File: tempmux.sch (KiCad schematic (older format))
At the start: 23 parts, among them J3 Conn_02x07_Counter_Clockwise, U12 CD74HC4067SM

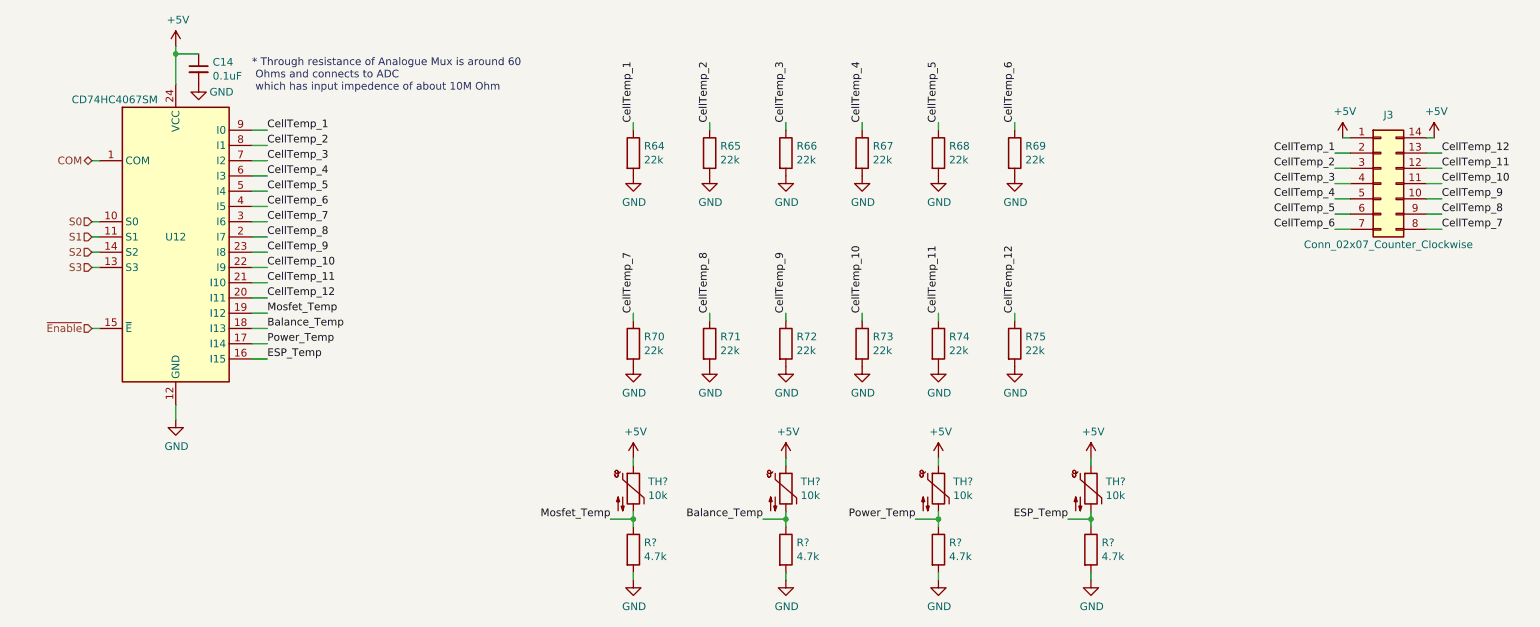
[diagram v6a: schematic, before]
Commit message: Added most footprints
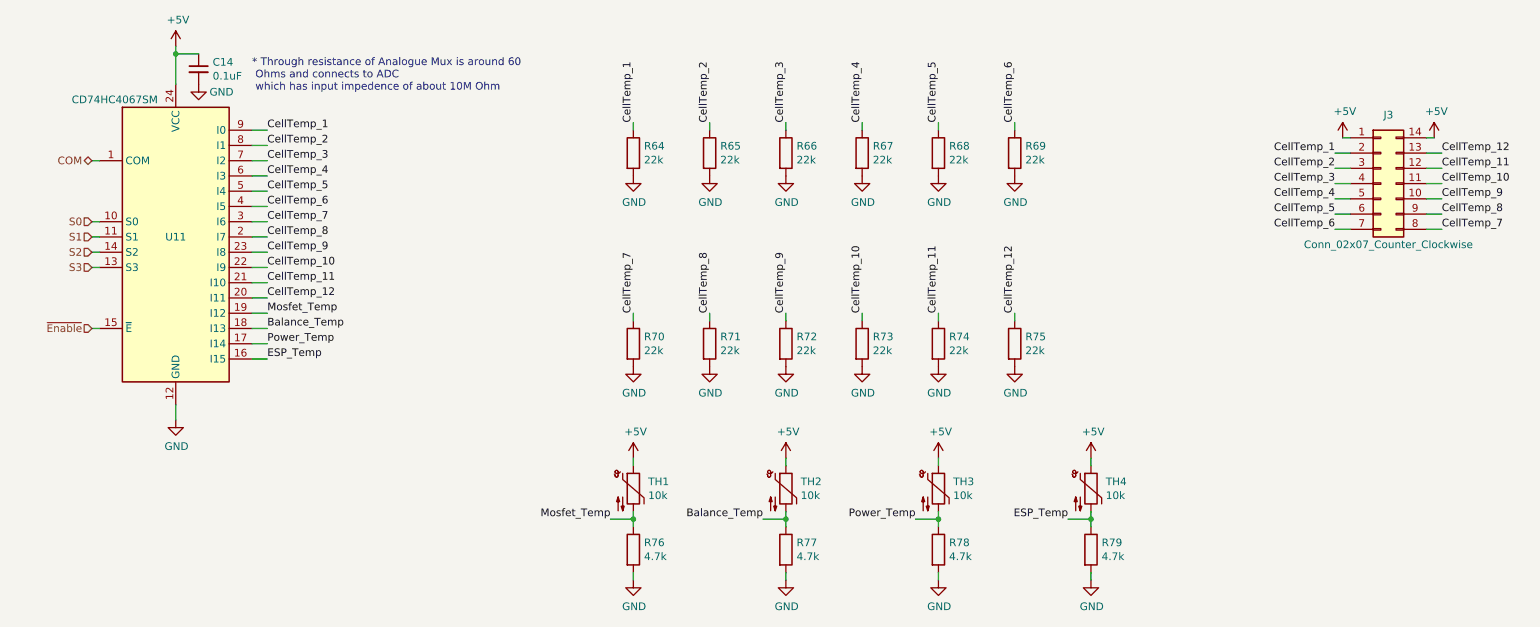
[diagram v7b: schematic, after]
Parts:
- C14: footprint (none) -> Capacitor_SMD:C_1206_3216Metric
- J3: footprint (none) -> Connector_PinHeader_2.54mm:PinHeader_2x07_P2.54mm_Vertical
- R64, R65, R66, R67, R68, R69, R70, R71, R72, R73, R74, R75: footprint (none) -> Resistor_SMD:R_0603_1608Metric_Pad1.05x0.95mm_HandSolder
- R76, R77, R78, R79: renamed from R?; footprint (none) -> Resistor_SMD:R_0603_1608Metric_Pad1.05x0.95mm_HandSolder
- TH1, TH2, TH3, TH4: renamed from TH?; footprint (none) -> Resistor_SMD:R_0201_0603Metric
- renumbered U12 to U11
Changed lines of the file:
@@
 P 2000 2200
 AR Path="/5F70A721/5F6868D3" Ref="U?"  Part="1"
-AR Path="/5F70B1A3/5F6868D3" Ref="U12"  Part="1"
-F 0 "U12" H 2000 2200 50  0000 C CNN
+AR Path="/5F70B1A3/5F6868D3" Ref="U11"  Part="1"
+F 0 "U11" H 2000 2200 50  0000 C CNN
 F 1 "CD74HC4067SM" H 1600 3100 50  0000 C CNN
 F 2 "Package_SO:SSOP-24_5.3x8.2mm_P0.65mm" H 3050 1200 50  0001 C CIN
@@
 F 0 "C14" H 2242 1146 50  0000 L CNN
 F 1 "0.1uF" H 2242 1055 50  0000 L CNN
-F 2 "" H 2150 1100 50  0001 C CNN
+F 2 "Capacitor_SMD:C_1206_3216Metric" H 2150 1100 50  0001 C CNN
 F 3 "~" H 2150 1100 50  0001 C CNN
 	1    2150 1100
@@
 F 0 "J3" H 9950 2300 50  0000 C CNN
 F 1 "Conn_02x07_Counter_Clockwise" H 9950 1450 50  0000 C CNN
-F 2 "" H 9900 1850 50  0001 C CNN
+F 2 "Connector_PinHeader_2.54mm:PinHeader_2x07_P2.54mm_Vertical" H 9900 1850 50  0001 C CNN
 F 3 "~" H 9900 1850 50  0001 C CNN
 	1    9900 1850
@@
 F 0 "R64" H 5070 1696 50  0000 L CNN
 F 1 "22k" H 5070 1605 50  0000 L CNN
-F 2 "" V 4930 1650 50  0001 C CNN
+F 2 "Resistor_SMD:R_0603_1608Metric_Pad1.05x0.95mm_HandSolder" V 4930 1650 50  0001 C CNN
 F 3 "~" H 5000 1650 50  0001 C CNN
 	1    5000 1650
@@
 F 0 "R65" H 5570 1696 50  0000 L CNN
 F 1 "22k" H 5570 1605 50  0000 L CNN
-F 2 "" V 5430 1650 50  0001 C CNN
+F 2 "Resistor_SMD:R_0603_1608Metric_Pad1.05x0.95mm_HandSolder" V 5430 1650 50  0001 C CNN
 F 3 "~" H 5500 1650 50  0001 C CNN
 	1    5500 1650
@@
 F 0 "R66" H 6070 1696 50  0000 L CNN
 F 1 "22k" H 6070 1605 50  0000 L CNN
-F 2 "" V 5930 1650 50  0001 C CNN
+F 2 "Resistor_SMD:R_0603_1608Metric_Pad1.05x0.95mm_HandSolder" V 5930 1650 50  0001 C CNN
 F 3 "~" H 6000 1650 50  0001 C CNN
 	1    6000 1650
@@
 F 0 "R67" H 6570 1696 50  0000 L CNN
 F 1 "22k" H 6570 1605 50  0000 L CNN
-F 2 "" V 6430 1650 50  0001 C CNN
+F 2 "Resistor_SMD:R_0603_1608Metric_Pad1.05x0.95mm_HandSolder" V 6430 1650 50  0001 C CNN
 F 3 "~" H 6500 1650 50  0001 C CNN
 	1    6500 1650
@@
 F 0 "R68" H 7070 1696 50  0000 L CNN
 F 1 "22k" H 7070 1605 50  0000 L CNN
-F 2 "" V 6930 1650 50  0001 C CNN
+F 2 "Resistor_SMD:R_0603_1608Metric_Pad1.05x0.95mm_HandSolder" V 6930 1650 50  0001 C CNN
 F 3 "~" H 7000 1650 50  0001 C CNN
 	1    7000 1650
@@
 F 0 "R69" H 7570 1696 50  0000 L CNN
 F 1 "22k" H 7570 1605 50  0000 L CNN
-F 2 "" V 7430 1650 50  0001 C CNN
+F 2 "Resistor_SMD:R_0603_1608Metric_Pad1.05x0.95mm_HandSolder" V 7430 1650 50  0001 C CNN
 F 3 "~" H 7500 1650 50  0001 C CNN
 	1    7500 1650
@@
 F 0 "R70" H 5070 2946 50  0000 L CNN
 F 1 "22k" H 5070 2855 50  0000 L CNN
-F 2 "" V 4930 2900 50  0001 C CNN
+F 2 "Resistor_SMD:R_0603_1608Metric_Pad1.05x0.95mm_HandSolder" V 4930 2900 50  0001 C CNN
 F 3 "~" H 5000 2900 50  0001 C CNN
 	1    5000 2900
@@
 F 0 "R71" H 5570 2946 50  0000 L CNN
 F 1 "22k" H 5570 2855 50  0000 L CNN
-F 2 "" V 5430 2900 50  0001 C CNN
+F 2 "Resistor_SMD:R_0603_1608Metric_Pad1.05x0.95mm_HandSolder" V 5430 2900 50  0001 C CNN
 F 3 "~" H 5500 2900 50  0001 C CNN
 	1    5500 2900
@@
 F 0 "R72" H 6070 2946 50  0000 L CNN
 F 1 "22k" H 6070 2855 50  0000 L CNN
-F 2 "" V 5930 2900 50  0001 C CNN
+F 2 "Resistor_SMD:R_0603_1608Metric_Pad1.05x0.95mm_HandSolder" V 5930 2900 50  0001 C CNN
 F 3 "~" H 6000 2900 50  0001 C CNN
 	1    6000 2900
@@
 F 0 "R73" H 6570 2946 50  0000 L CNN
 F 1 "22k" H 6570 2855 50  0000 L CNN
-F 2 "" V 6430 2900 50  0001 C CNN
+F 2 "Resistor_SMD:R_0603_1608Metric_Pad1.05x0.95mm_HandSolder" V 6430 2900 50  0001 C CNN
 F 3 "~" H 6500 2900 50  0001 C CNN
 	1    6500 2900
@@
 F 0 "R74" H 7070 2946 50  0000 L CNN
 F 1 "22k" H 7070 2855 50  0000 L CNN
-F 2 "" V 6930 2900 50  0001 C CNN
+F 2 "Resistor_SMD:R_0603_1608Metric_Pad1.05x0.95mm_HandSolder" V 6930 2900 50  0001 C CNN
 F 3 "~" H 7000 2900 50  0001 C CNN
 	1    7000 2900
@@
 F 0 "R75" H 7570 2946 50  0000 L CNN
 F 1 "22k" H 7570 2855 50  0000 L CNN
-F 2 "" V 7430 2900 50  0001 C CNN
+F 2 "Resistor_SMD:R_0603_1608Metric_Pad1.05x0.95mm_HandSolder" V 7430 2900 50  0001 C CNN
 F 3 "~" H 7500 2900 50  0001 C CNN
 	1    7500 2900
@@
 	2500 2600 2600 2600
 $Comp
-L Device:Thermistor_NTC TH?
+L Device:Thermistor_NTC TH1
 U 1 1 5F26609F
 P 5000 3850
-F 0 "TH?" H 5097 3896 50  0000 L CNN
+F 0 "TH1" H 5097 3896 50  0000 L CNN
 F 1 "10k" H 5097 3805 50  0000 L CNN
-F 2 "" H 5000 3900 50  0001 C CNN
+F 2 "Resistor_SMD:R_0201_0603Metric" H 5000 3900 50  0001 C CNN
 F 3 "~" H 5000 3900 50  0001 C CNN
 	1    5000 3850
@@
 $EndComp
 $Comp
-L Device:R R?
+L Device:R R76
 U 1 1 5F2670CB
 P 5000 4250
-F 0 "R?" H 5070 4296 50  0000 L CNN
+F 0 "R76" H 5070 4296 50  0000 L CNN
 F 1 "4.7k" H 5070 4205 50  0000 L CNN
-F 2 "" V 4930 4250 50  0001 C CNN
+F 2 "Resistor_SMD:R_0603_1608Metric_Pad1.05x0.95mm_HandSolder" V 4930 4250 50  0001 C CNN
 F 3 "~" H 5000 4250 50  0001 C CNN
 	1    5000 4250
@@
 P 5000 4450
 AR Path="/5F70A721/5F26879D" Ref="#PWR?"  Part="1"
-AR Path="/5F70B1A3/5F26879D" Ref="#PWR?"  Part="1"
-F 0 "#PWR?" H 5000 4200 50  0001 C CNN
+AR Path="/5F70B1A3/5F26879D" Ref="#PWR083"  Part="1"
+F 0 "#PWR083" H 5000 4200 50  0001 C CNN
 F 1 "GND" H 5005 4277 50  0000 C CNN
 F 2 "" H 5000 4450 50  0001 C CNN
@@
 P 5000 3650
 AR Path="/5F70A721/5F269BD4" Ref="#PWR?"  Part="1"
-AR Path="/5F70B1A3/5F269BD4" Ref="#PWR?"  Part="1"
-F 0 "#PWR?" H 5000 3500 50  0001 C CNN
+AR Path="/5F70B1A3/5F269BD4" Ref="#PWR079"  Part="1"
+F 0 "#PWR079" H 5000 3500 50  0001 C CNN
 F 1 "+5V" H 5015 3823 50  0000 C CNN
 F 2 "" H 5000 3650 50  0001 C CNN
@@
 	5000 3650 5000 3700
 $Comp
-L Device:Thermistor_NTC TH?
+L Device:Thermistor_NTC TH2
 U 1 1 5F26E197
 P 6000 3850
-F 0 "TH?" H 6097 3896 50  0000 L CNN
+F 0 "TH2" H 6097 3896 50  0000 L CNN
 F 1 "10k" H 6097 3805 50  0000 L CNN
-F 2 "" H 6000 3900 50  0001 C CNN
+F 2 "Resistor_SMD:R_0201_0603Metric" H 6000 3900 50  0001 C CNN
 F 3 "~" H 6000 3900 50  0001 C CNN
 	1    6000 3850
@@
 $EndComp
 $Comp
-L Device:R R?
+L Device:R R77
 U 1 1 5F26E19D
 P 6000 4250
-F 0 "R?" H 6070 4296 50  0000 L CNN
+F 0 "R77" H 6070 4296 50  0000 L CNN
 F 1 "4.7k" H 6070 4205 50  0000 L CNN
-F 2 "" V 5930 4250 50  0001 C CNN
+F 2 "Resistor_SMD:R_0603_1608Metric_Pad1.05x0.95mm_HandSolder" V 5930 4250 50  0001 C CNN
 F 3 "~" H 6000 4250 50  0001 C CNN
 	1    6000 4250
@@
 P 6000 4450
 AR Path="/5F70A721/5F26E1A4" Ref="#PWR?"  Part="1"
-AR Path="/5F70B1A3/5F26E1A4" Ref="#PWR?"  Part="1"
-F 0 "#PWR?" H 6000 4200 50  0001 C CNN
+AR Path="/5F70B1A3/5F26E1A4" Ref="#PWR084"  Part="1"
+F 0 "#PWR084" H 6000 4200 50  0001 C CNN
 F 1 "GND" H 6005 4277 50  0000 C CNN
 F 2 "" H 6000 4450 50  0001 C CNN
@@
 P 6000 3650
 AR Path="/5F70A721/5F26E1AB" Ref="#PWR?"  Part="1"
-AR Path="/5F70B1A3/5F26E1AB" Ref="#PWR?"  Part="1"
-F 0 "#PWR?" H 6000 3500 50  0001 C CNN
+AR Path="/5F70B1A3/5F26E1AB" Ref="#PWR080"  Part="1"
+F 0 "#PWR080" H 6000 3500 50  0001 C CNN
 F 1 "+5V" H 6015 3823 50  0000 C CNN
 F 2 "" H 6000 3650 50  0001 C CNN
@@
 	6000 3650 6000 3700
 $Comp
-L Device:Thermistor_NTC TH?
+L Device:Thermistor_NTC TH3
 U 1 1 5F2705BF
 P 7000 3850
-F 0 "TH?" H 7097 3896 50  0000 L CNN
+F 0 "TH3" H 7097 3896 50  0000 L CNN
 F 1 "10k" H 7097 3805 50  0000 L CNN
-F 2 "" H 7000 3900 50  0001 C CNN
+F 2 "Resistor_SMD:R_0201_0603Metric" H 7000 3900 50  0001 C CNN
 F 3 "~" H 7000 3900 50  0001 C CNN
 	1    7000 3850
@@
 $EndComp
 $Comp
-L Device:R R?
+L Device:R R78
 U 1 1 5F2705C5
 P 7000 4250
-F 0 "R?" H 7070 4296 50  0000 L CNN
+F 0 "R78" H 7070 4296 50  0000 L CNN
 F 1 "4.7k" H 7070 4205 50  0000 L CNN
-F 2 "" V 6930 4250 50  0001 C CNN
+F 2 "Resistor_SMD:R_0603_1608Metric_Pad1.05x0.95mm_HandSolder" V 6930 4250 50  0001 C CNN
 F 3 "~" H 7000 4250 50  0001 C CNN
 	1    7000 4250
@@
 P 7000 4450
 AR Path="/5F70A721/5F2705CC" Ref="#PWR?"  Part="1"
-AR Path="/5F70B1A3/5F2705CC" Ref="#PWR?"  Part="1"
-F 0 "#PWR?" H 7000 4200 50  0001 C CNN
+AR Path="/5F70B1A3/5F2705CC" Ref="#PWR085"  Part="1"
+F 0 "#PWR085" H 7000 4200 50  0001 C CNN
 F 1 "GND" H 7005 4277 50  0000 C CNN
 F 2 "" H 7000 4450 50  0001 C CNN
@@
 P 7000 3650
 AR Path="/5F70A721/5F2705D3" Ref="#PWR?"  Part="1"
-AR Path="/5F70B1A3/5F2705D3" Ref="#PWR?"  Part="1"
-F 0 "#PWR?" H 7000 3500 50  0001 C CNN
+AR Path="/5F70B1A3/5F2705D3" Ref="#PWR081"  Part="1"
+F 0 "#PWR081" H 7000 3500 50  0001 C CNN
 F 1 "+5V" H 7015 3823 50  0000 C CNN
 F 2 "" H 7000 3650 50  0001 C CNN
@@
 	7000 3650 7000 3700
 $Comp
-L Device:Thermistor_NTC TH?
+L Device:Thermistor_NTC TH4
 U 1 1 5F272D59
 P 8000 3850
-F 0 "TH?" H 8097 3896 50  0000 L CNN
+F 0 "TH4" H 8097 3896 50  0000 L CNN
 F 1 "10k" H 8097 3805 50  0000 L CNN
-F 2 "" H 8000 3900 50  0001 C CNN
+F 2 "Resistor_SMD:R_0201_0603Metric" H 8000 3900 50  0001 C CNN
 F 3 "~" H 8000 3900 50  0001 C CNN
 	1    8000 3850
@@
 $EndComp
 $Comp
-L Device:R R?
+L Device:R R79
 U 1 1 5F272D5F
 P 8000 4250
-F 0 "R?" H 8070 4296 50  0000 L CNN
+F 0 "R79" H 8070 4296 50  0000 L CNN
 F 1 "4.7k" H 8070 4205 50  0000 L CNN
-F 2 "" V 7930 4250 50  0001 C CNN
+F 2 "Resistor_SMD:R_0603_1608Metric_Pad1.05x0.95mm_HandSolder" V 7930 4250 50  0001 C CNN
 F 3 "~" H 8000 4250 50  0001 C CNN
 	1    8000 4250
@@
 P 8000 4450
 AR Path="/5F70A721/5F272D66" Ref="#PWR?"  Part="1"
-AR Path="/5F70B1A3/5F272D66" Ref="#PWR?"  Part="1"
-F 0 "#PWR?" H 8000 4200 50  0001 C CNN
+AR Path="/5F70B1A3/5F272D66" Ref="#PWR086"  Part="1"
+F 0 "#PWR086" H 8000 4200 50  0001 C CNN
 F 1 "GND" H 8005 4277 50  0000 C CNN
 F 2 "" H 8000 4450 50  0001 C CNN
@@
 P 8000 3650
 AR Path="/5F70A721/5F272D6D" Ref="#PWR?"  Part="1"
-AR Path="/5F70B1A3/5F272D6D" Ref="#PWR?"  Part="1"
-F 0 "#PWR?" H 8000 3500 50  0001 C CNN
+AR Path="/5F70B1A3/5F272D6D" Ref="#PWR082"  Part="1"
+F 0 "#PWR082" H 8000 3500 50  0001 C CNN
 F 1 "+5V" H 8015 3823 50  0000 C CNN
 F 2 "" H 8000 3650 50  0001 C CNN

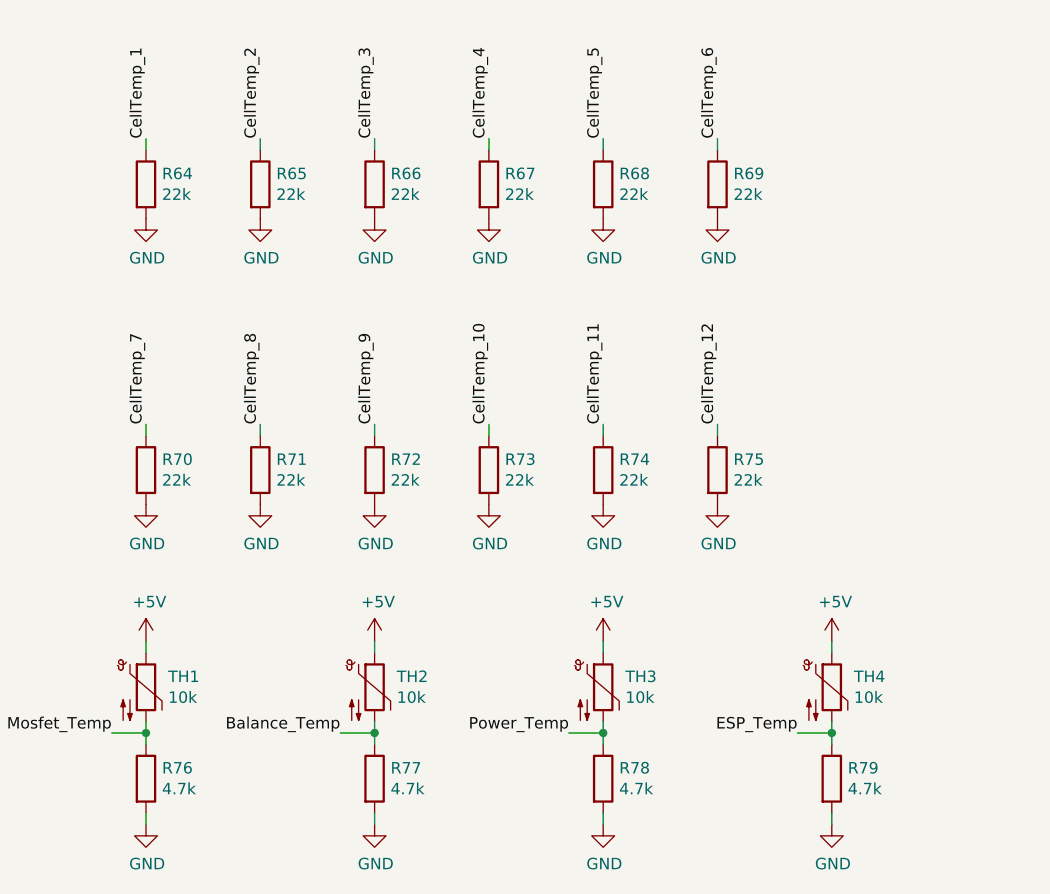
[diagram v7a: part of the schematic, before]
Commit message: Switched to lower GPIO pin part to save space
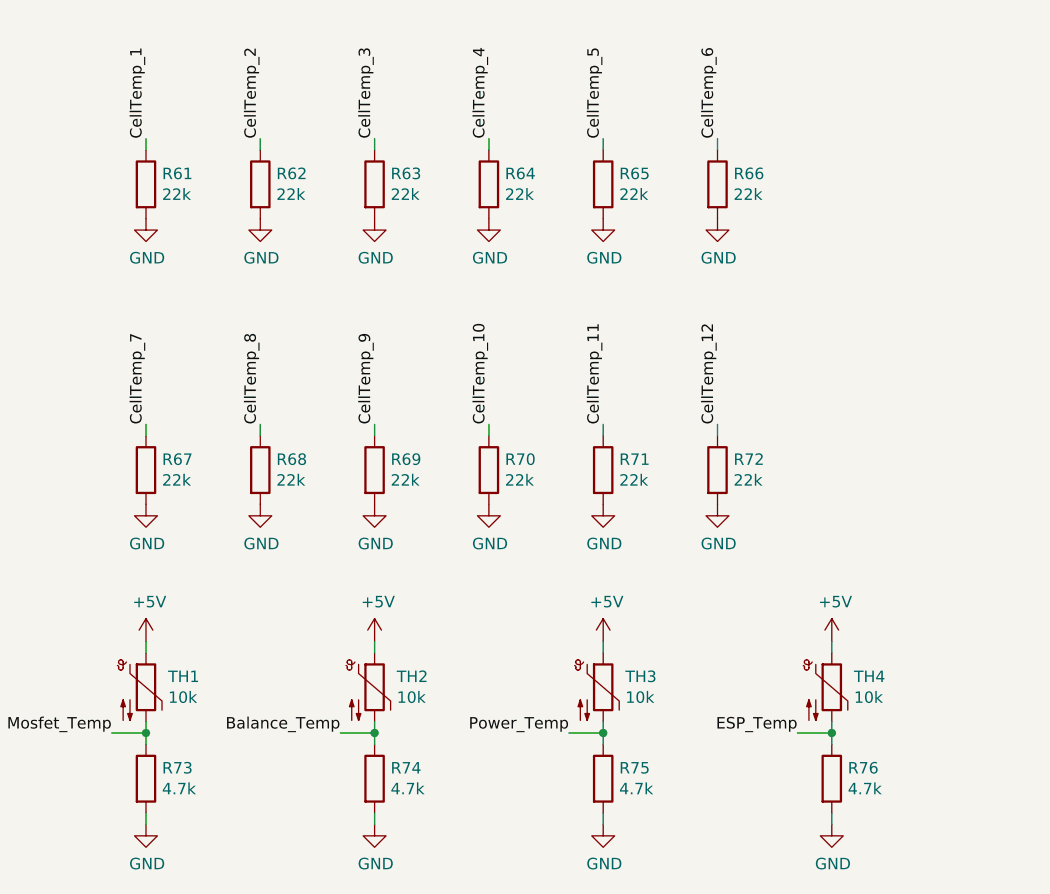
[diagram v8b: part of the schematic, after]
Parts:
- renumbered R64 to R61, R65 to R62, R66 to R63, R67 to R64, R68 to R65, R69 to R66, R70 to R67, R71 to R68, R72 to R69, R73 to R70, R74 to R71, R75 to R72, R76 to R73, R77 to R74, R78 to R75, R79 to R76
